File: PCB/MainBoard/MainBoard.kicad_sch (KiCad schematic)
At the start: 4 parts, among them U3 STM32F103C8Tx

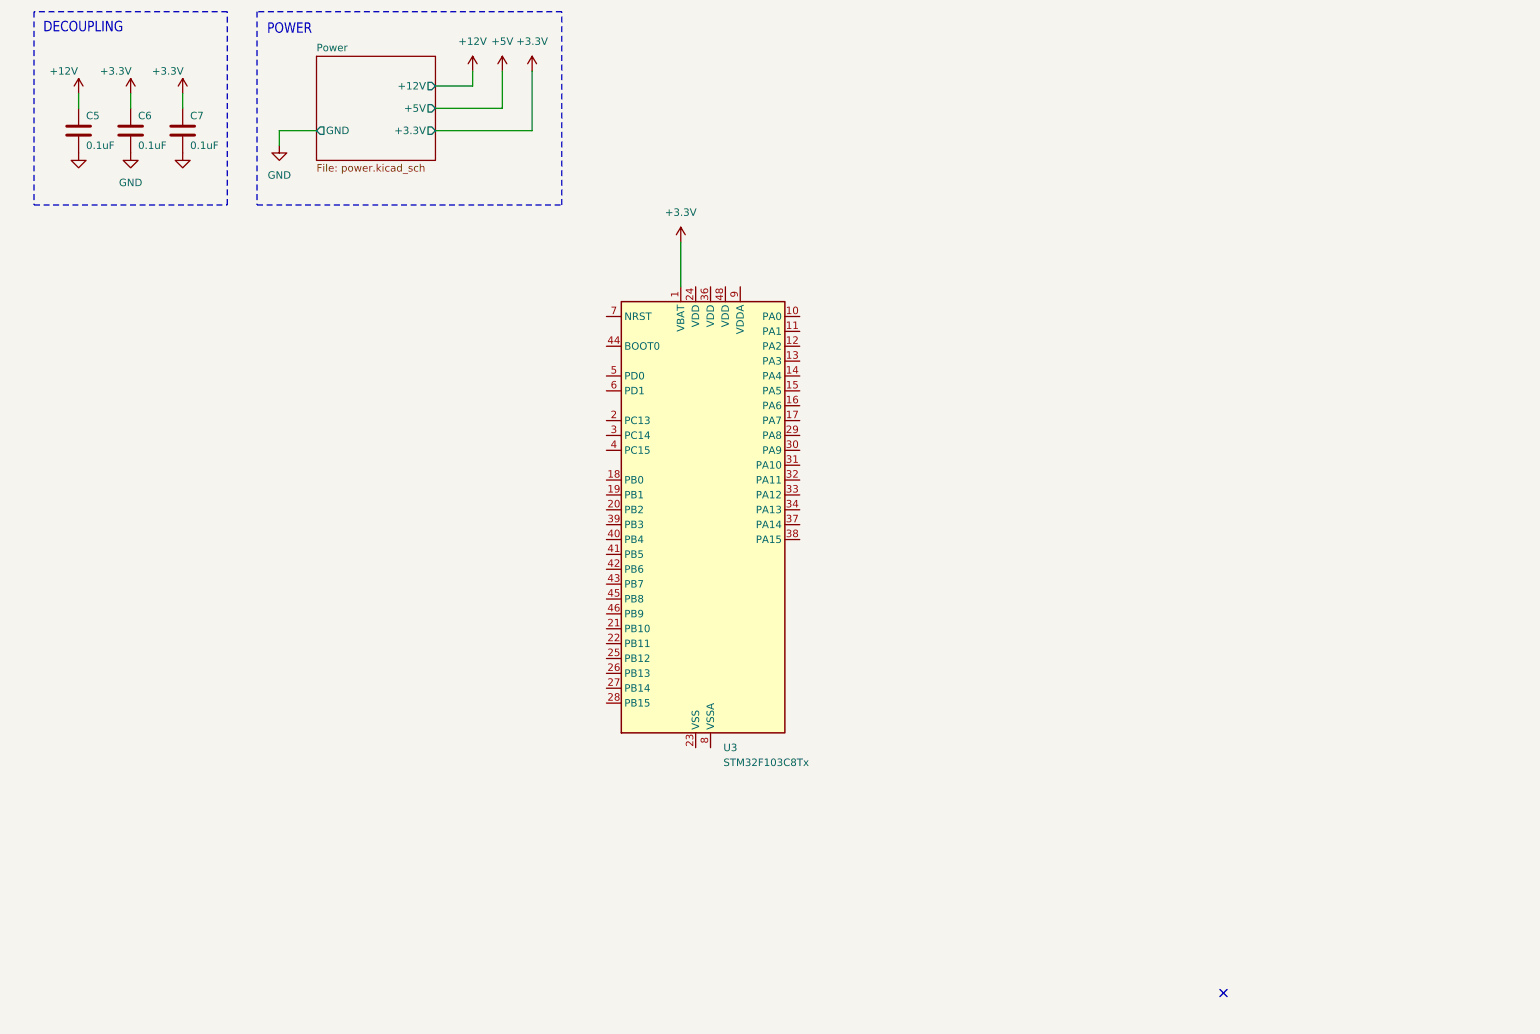
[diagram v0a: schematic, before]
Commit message: updating pcb
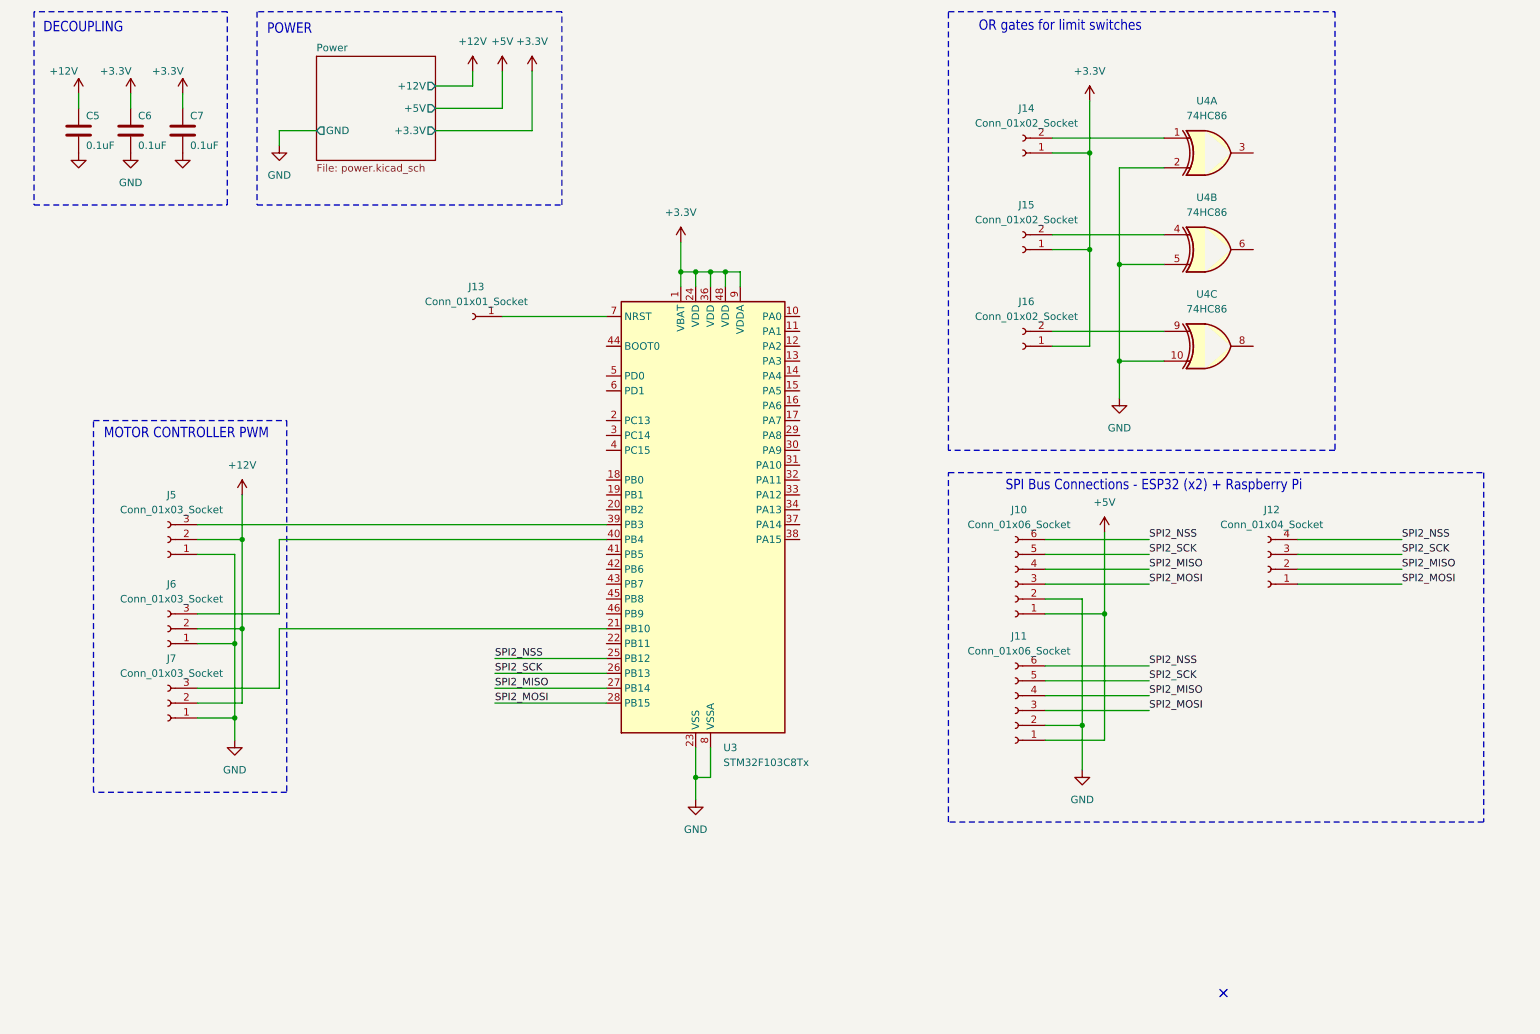
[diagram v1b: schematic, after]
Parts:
- added J10, J11: Conn_01x06_Socket, symbol Connector:Conn_01x06_Socket
- added J12: Conn_01x04_Socket, symbol Connector:Conn_01x04_Socket
- added J13: Conn_01x01_Socket, symbol Connector:Conn_01x01_Socket
- added J14, J15, J16: Conn_01x02_Socket, symbol Connector:Conn_01x02_Socket
- added J5, J6, J7: Conn_01x03_Socket, symbol Connector:Conn_01x03_Socket
- added U4: 74HC86, symbol 74xx:74HC86
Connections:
- net +12V: now also J5.2 (Pin_2), J6.2 (Pin_2), J7.2 (Pin_2)
- net +3.3V: now also U3.24 (VDD), U3.36 (VDD), U3.48 (VDD), U3.9 (VDDA), J14.1 (Pin_1), J15.1 (Pin_1), J16.1 (Pin_1)
- net +5V: now also J10.1 (Pin_1), J11.1 (Pin_1)
- net GND: now also U3.23 (VSS), U3.35 (VSS), U3.47 (VSS), U3.8 (VSSA), J10.2 (Pin_2), J11.2 (Pin_2), J5.1 (Pin_1), J6.1 (Pin_1), J7.1 (Pin_1), U4.10, U4.2, U4.5
- net at U3.21 (PB10): now also J7.3 (Pin_3)
- net SPI2_NSS: now reaches U3.25 (PB12)
- net SPI2_NSS: now also J10.6 (Pin_6), J11.6 (Pin_6), J12.4 (Pin_4)
- net SPI2_SCK: now reaches U3.26 (PB13)
- net SPI2_SCK: now also J10.5 (Pin_5), J11.5 (Pin_5), J12.3 (Pin_3)
- net SPI2_MISO: now reaches U3.27 (PB14)
- net SPI2_MISO: now also J10.4 (Pin_4), J11.4 (Pin_4), J12.2 (Pin_2)
- net SPI2_MOSI: now reaches U3.28 (PB15)
- net SPI2_MOSI: now also J10.3 (Pin_3), J11.3 (Pin_3), J12.1 (Pin_1)
- net at U3.39 (PB3): now also J5.3 (Pin_3)
- net at U3.40 (PB4): now also J6.3 (Pin_3)
- net at U3.7 (NRST): now also J13.1 (Pin_1)
- new net: J14.2 (Pin_2), U4.1
- new net: J15.2 (Pin_2), U4.4
- new net: J16.2 (Pin_2), U4.9
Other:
- note added: "MOTOR CONTROLLER PWM"
- note added: "OR gates for limit switches"
- note added: "SPI Bus Connections - ESP32 (x2) + Raspberry Pi"

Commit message: updating progress
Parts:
- added J18, J19, J20: Conn_01x04_Socket, symbol Connector:Conn_01x04_Socket
- renumbered C5 to C3, C6 to C4, C7 to C5
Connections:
- net +3.3V: now also J18.1 (Pin_1), J19.1 (Pin_1), J20.1 (Pin_1)
- net GND: now also J18.2 (Pin_2), J19.2 (Pin_2), J20.2 (Pin_2)
- net ME1_ChA: now reaches U3.12 (PA2)
- net ME1_ChA: now also J19.3 (Pin_3)
- net ME1_ChB: now reaches U3.13 (PA3)
- net ME1_ChB: now also J19.4 (Pin_4)
- net ME3_ChA: now reaches U3.16 (PA6)
- net ME3_ChA: now also J20.3 (Pin_3)
- net ME3_ChB: now reaches U3.17 (PA7)
- net ME3_ChB: now also J20.4 (Pin_4)
- net ME2_ChA: now reaches U3.18 (PB0)
- net ME2_ChA: now also J18.3 (Pin_3)
- net ME2_ChB: now reaches U3.19 (PB1)
- net ME2_ChB: now also J18.4 (Pin_4)
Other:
- note added: "MOTOR ENCODERS"
- note added: "OR gates for limit switches (NEED TO FIX)"
- note removed: "OR gates for limit switches"
- moved on the sheet: J5, J6, J7

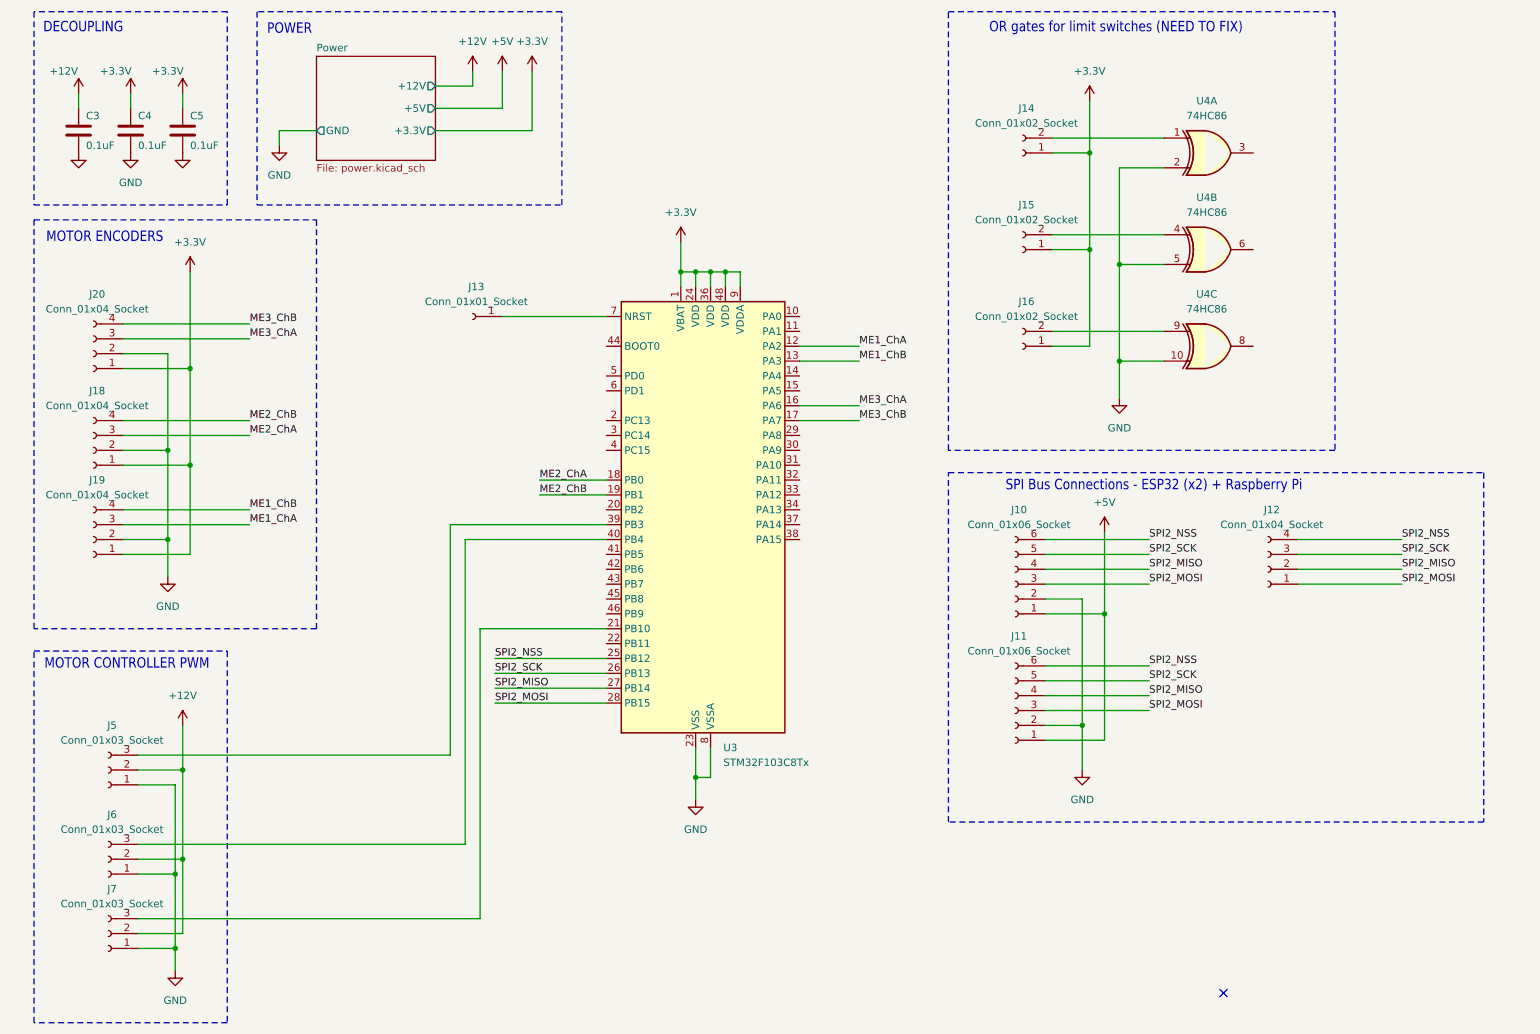
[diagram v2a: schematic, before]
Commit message: updating power schematics, and power lines
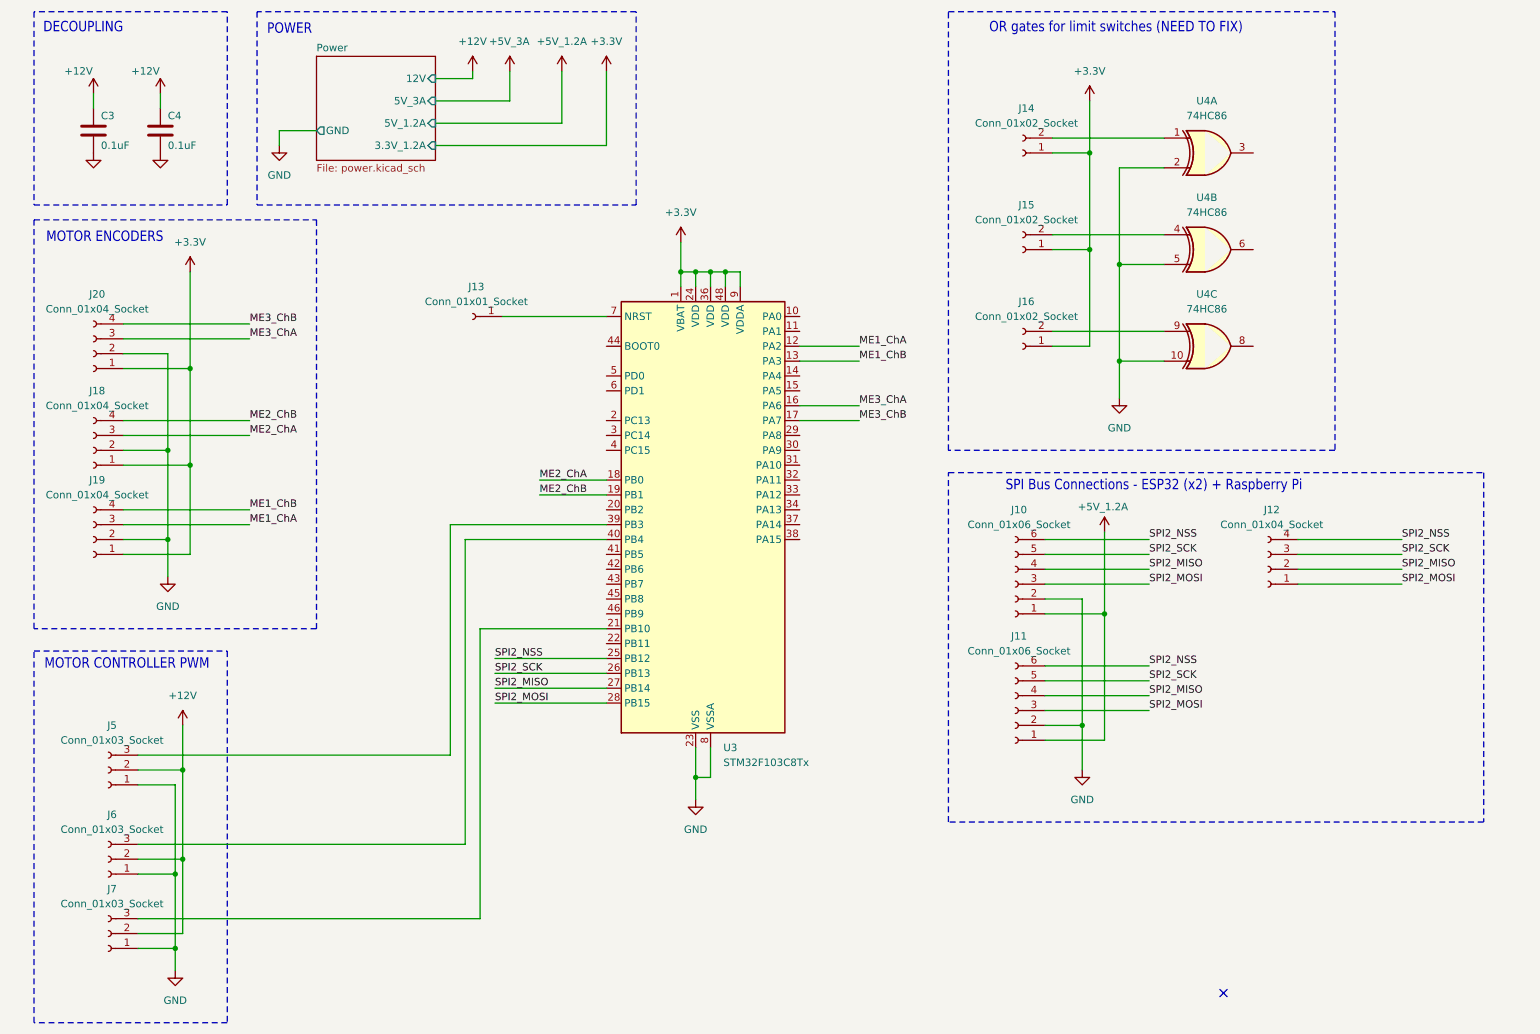
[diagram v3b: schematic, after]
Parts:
- removed C5: 0.1uF, Capacitor_SMD:C_0805_2012Metric_Pad1.18x1.45mm_HandSolder, symbol Device:C
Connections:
- net +12V: now also C4.1
- net +3.3V: no longer C4.1
- net +5V renamed +5V_1.2A
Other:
- sheet Power ports: added 12V, 3.3V_1.2A, 5V_1.2A, 5V_3A; removed +12V, +3.3V, +5V
- moved on the sheet: C3

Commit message: passed ERC in schematic
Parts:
- removed J13: Conn_01x01_Socket, symbol Connector:Conn_01x01_Socket
- removed J14, J15, J16: Conn_01x02_Socket, symbol Connector:Conn_01x02_Socket
- removed U4: 74HC86, symbol 74xx:74HC86
- added C5: 0.1uF, Capacitor_SMD:C_1206_3216Metric_Pad1.33x1.80mm_HandSolder, symbol Device:C
- added SW1: SW_Push_Dual, Button_Switch_THT:SW_PUSH_6mm_H7.3mm, symbol Switch:SW_Push_Dual
- C3, C4: footprint Capacitor_SMD:C_0805_2012Metric_Pad1.18x1.45mm_HandSolder -> Capacitor_SMD:C_1206_3216Metric_Pad1.33x1.80mm_HandSolder
- J10, J11: footprint (none) -> Connector_PinHeader_2.54mm:PinHeader_1x06_P2.54mm_Vertical
- J12: footprint (none) -> Connector_PinHeader_2.54mm:PinHeader_1x04_P2.54mm_Vertical
- J18, J19, J20: footprint (none) -> Connector_JST:JST_XH_B4B-XH-A_1x04_P2.50mm_Vertical
- J5, J6, J7: footprint (none) -> Connector_PinHeader_2.54mm:PinHeader_1x03_P2.54mm_Vertical
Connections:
- net GND: now also C5.2, SW1.1, SW1.3
- net LimitSwitchORGates/OR3 Output: now reaches U3.22 (PB11)
- net at U3.7 (NRST): now also C5.1, SW1.2, SW1.4
- net +3.3V renamed +3.3V_1.2A
- net +3.3V_1.2A: no longer U3.1 (VBAT)
- no-connect marks 1 -> 25
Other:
- added sheet LimitSwitchORGates (LimitSwitchOR.kicad_sch)
- sheet Power ports: added +12V, +3.3V_1.2A, +5V_1.2A, +5V_3A; removed 12V, 3.3V_1.2A, 5V_1.2A, 5V_3A
- note added: "LIMIT SWITCH ORs"
- note removed: "OR gates for limit switches (NEED TO FIX)"
- moved on the sheet: J10, J11, J12, J18, J19, J20

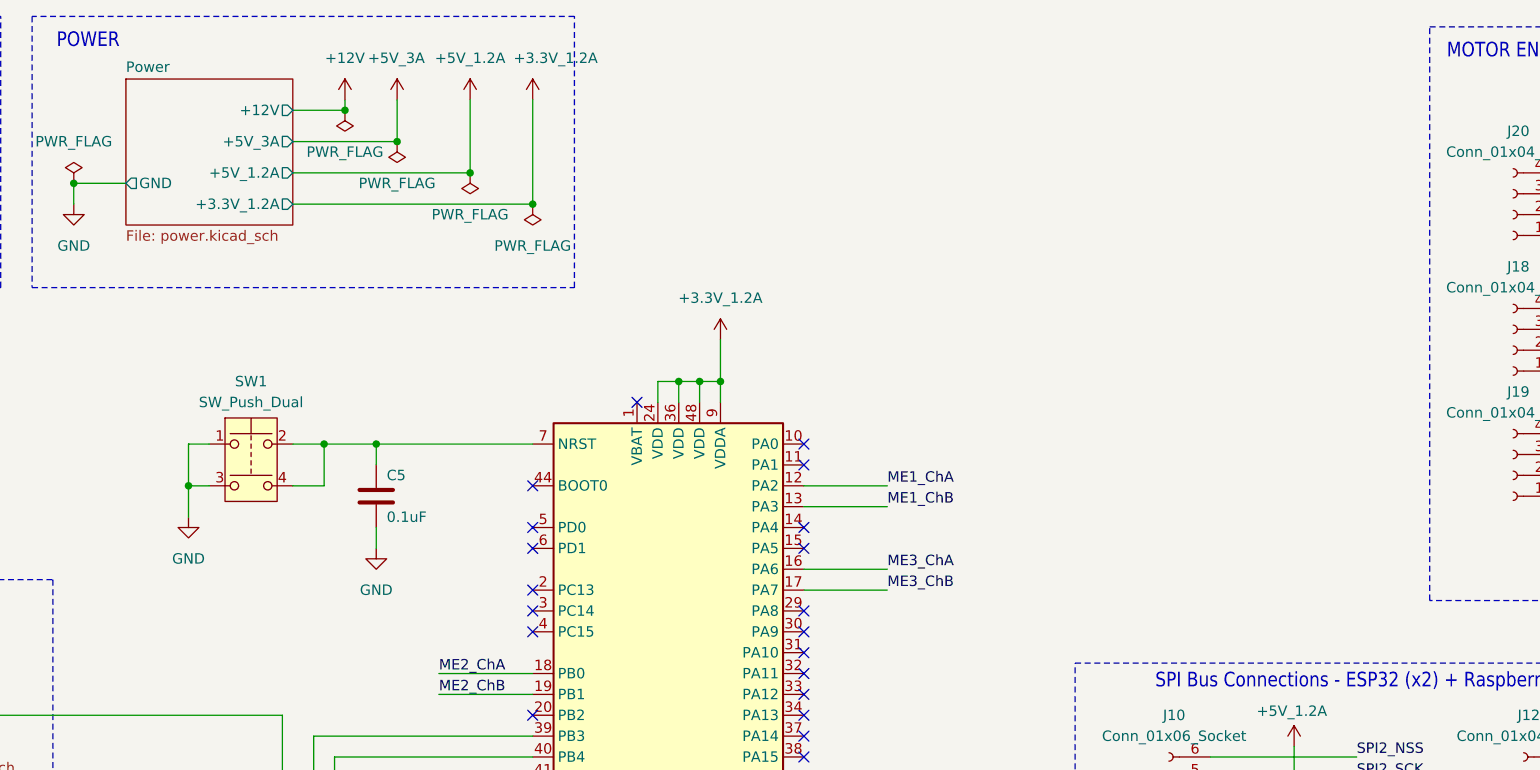
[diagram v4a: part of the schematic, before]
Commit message: began placing components - motor connectors, 12V in, mounting holes
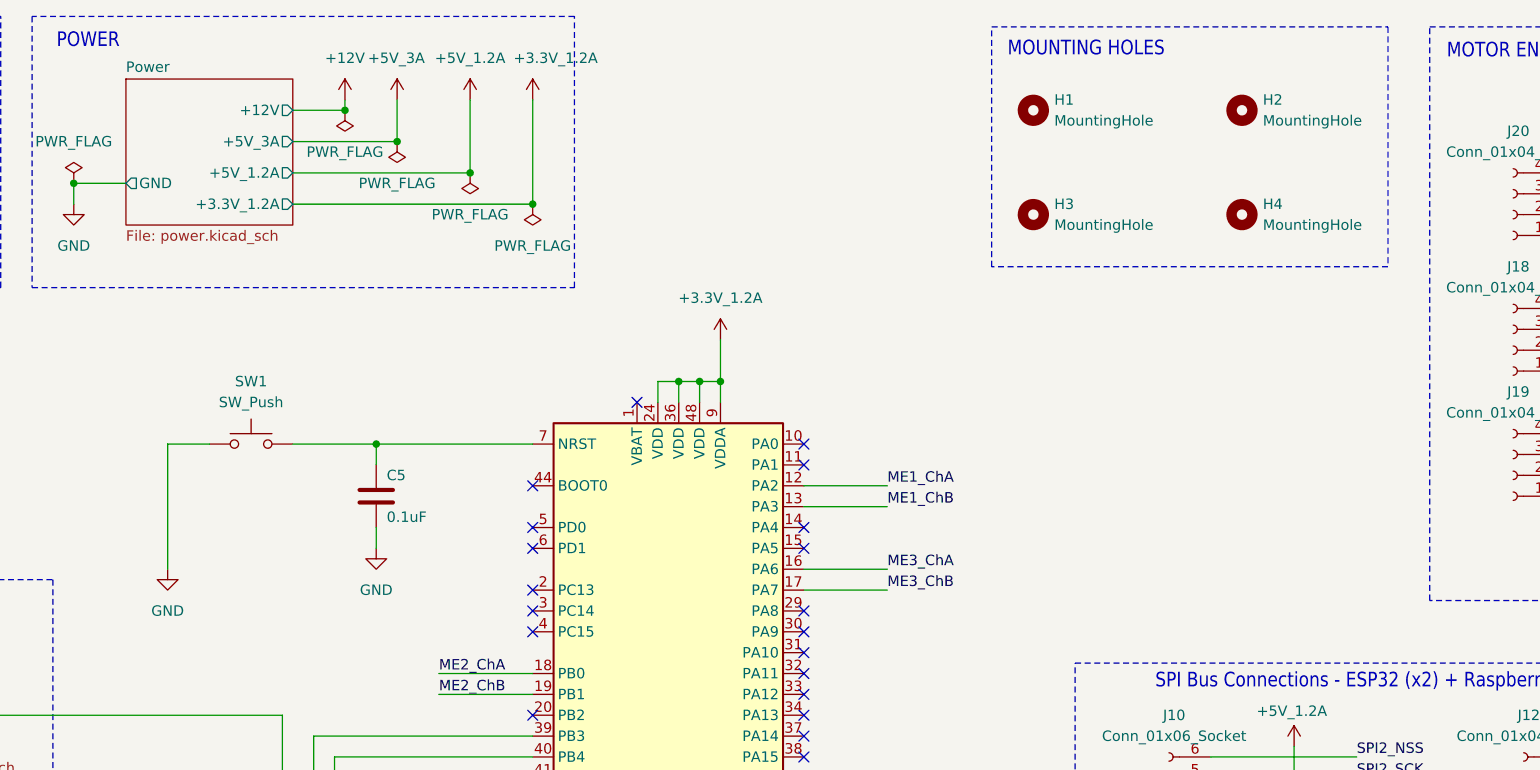
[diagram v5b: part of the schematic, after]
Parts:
- removed SW1: SW_Push_Dual, Button_Switch_THT:SW_PUSH_6mm_H7.3mm, symbol Switch:SW_Push_Dual
- added H1, H2, H3, H4: MountingHole, MountingHole:MountingHole_5mm, symbol Mechanical:MountingHole
- added SW1: SW_Push, Button_Switch_THT:SW_PUSH_6mm_H7.3mm, symbol Switch:SW_Push
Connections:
- net GND: now also SW1.1
- net at C5.1, U3.7 (NRST): now also SW1.2
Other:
- note added: "MOUNTING HOLES"
